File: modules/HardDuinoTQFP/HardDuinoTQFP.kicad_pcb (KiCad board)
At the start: 2 copper layers, 40.6 x 40.6 mm, 6 parts, among them J1 Conn_01x10_Male, J2 Conn_01x10_Male

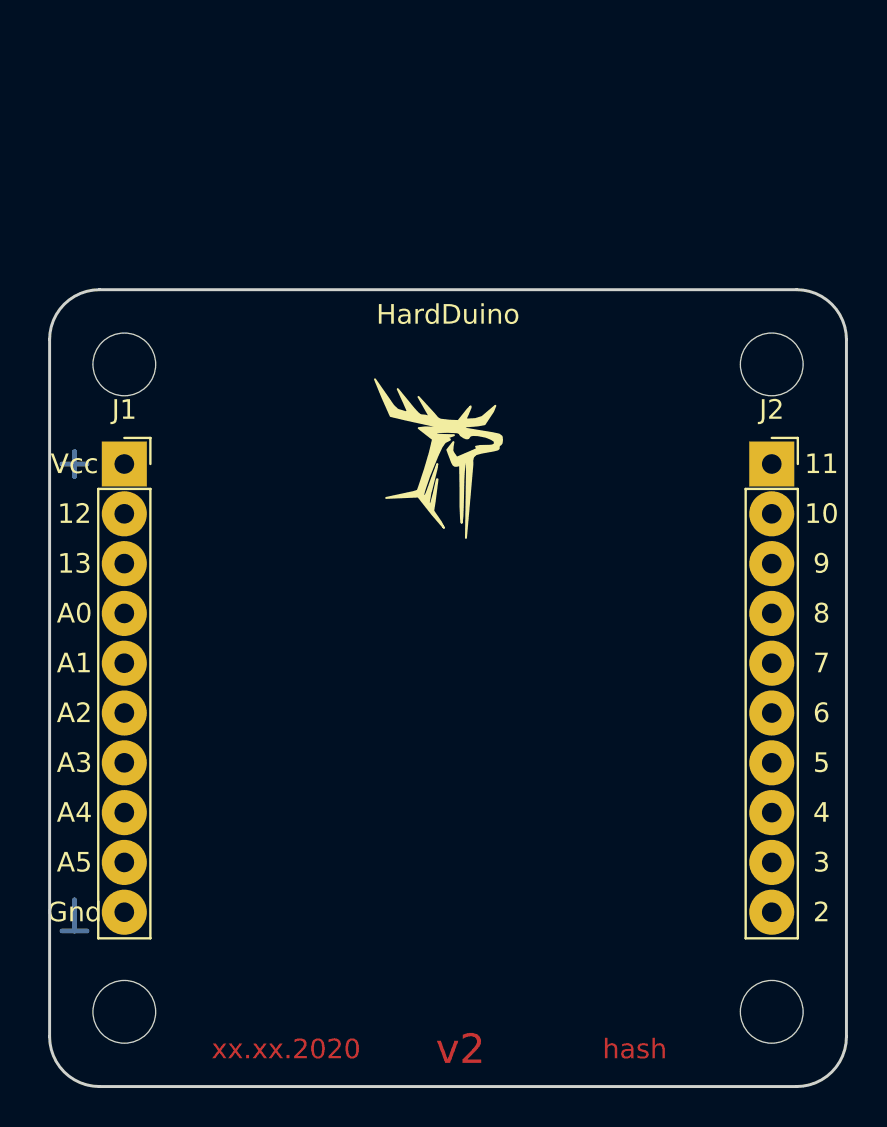
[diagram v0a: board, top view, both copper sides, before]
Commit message: HardDuino TQFP is ready
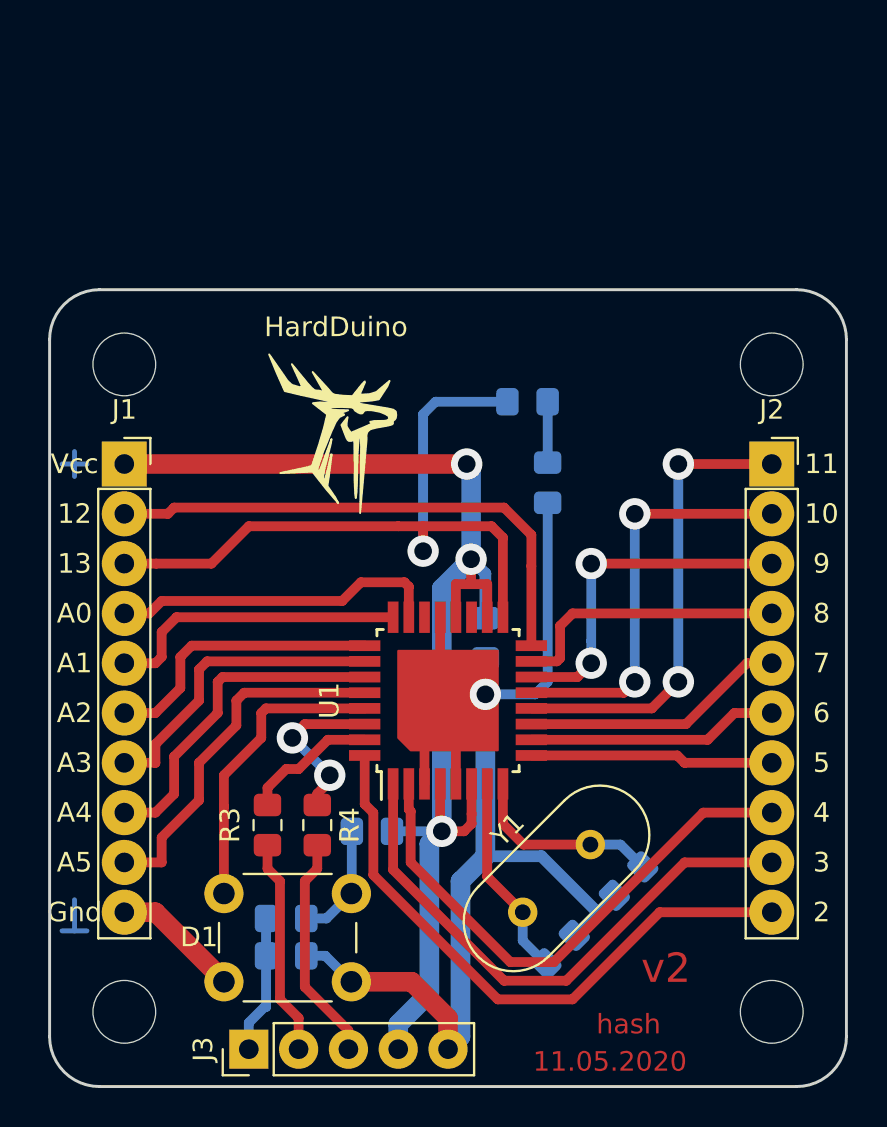
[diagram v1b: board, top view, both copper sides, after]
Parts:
- added C1: 0.1uF, Capacitor_SMD:C_0805_2012Metric_Pad1.15x1.40mm_HandSolder, B.Cu at (101.0, 82.9)
- added C2: 22pF, Capacitor_SMD:C_0805_2012Metric_Pad1.15x1.40mm_HandSolder, B.Cu at (114.9, 84.5)
- added C3: 22pF, Capacitor_SMD:C_0805_2012Metric_Pad1.15x1.40mm_HandSolder, B.Cu at (118.4, 81.0)
- added C4: C, Capacitor_SMD:C_0805_2012Metric_Pad1.15x1.40mm_HandSolder, B.Cu at (111.1, 68.6)
- added D1: 6x6-tact-btn, CommonLibrary:6x6-tact-btn, F.Cu at (97.8, 81.6)
- added D2: LED, LED_SMD:LED_0805_2012Metric_Pad1.15x1.40mm_HandSolder, B.Cu at (113.3, 56.5)
- added J3: Conn_01x05_Male, Connector_PinHeader_2.54mm:PinHeader_1x05_P2.54mm_Vertical, F.Cu at (99.1, 89.5)
- added R1: 1k, Resistor_SMD:R_0805_2012Metric_Pad1.15x1.40mm_HandSolder, B.Cu at (114.3, 60.6)
- added R2: 1k, Resistor_SMD:R_0805_2012Metric_Pad1.15x1.40mm_HandSolder, B.Cu at (101.0, 84.8)
- added R3: 1k, Resistor_SMD:R_0805_2012Metric_Pad1.15x1.40mm_HandSolder, F.Cu at (100.0, 78.1)
- added R4: 1k, Resistor_SMD:R_0805_2012Metric_Pad1.15x1.40mm_HandSolder, F.Cu at (102.6, 78.1)
- added R5: 10k, Resistor_SMD:R_0805_2012Metric_Pad1.15x1.40mm_HandSolder, B.Cu at (105.3, 78.4)
- added U1: ATmega328P-AU, Package_QFP:TQFP-32_7x7mm_P0.8mm, F.Cu at (109.2, 71.8)
- added Y1: 16MHz, Crystal:Crystal_HC49-U_Vertical, F.Cu at (113.0, 82.5)
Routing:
- net GND: track 0.00 -> 78.8 mm, vias 0 -> 1
- net VCC: track 0.00 -> 67.5 mm, vias 0 -> 3
- net /13: track 0.00 -> 37.2 mm, vias 0 -> 1
- net /2: track 0.00 -> 31.1 mm
- net /3: track 0.00 -> 28.5 mm
- net /4: track 0.00 -> 27.7 mm
- net /12: track 0.00 -> 27.1 mm
- net /11: track 0.00 -> 23.9 mm, vias 0 -> 2
- net Net-(C1-Pad1): track 0.00 -> 21.4 mm
- net /10: track 0.00 -> 21.1 mm, vias 0 -> 2
- net /A5: track 0.00 -> 18.4 mm
- net /9: track 0.00 -> 17.6 mm, vias 0 -> 2
- net /A4: track 0.00 -> 17.2 mm
- net /A0: track 0.00 -> 16.8 mm
- net /A3: track 0.00 -> 15.9 mm
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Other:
- board text added: "11.05.2020"
- board text removed: "xx.xx.2020"

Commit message: HardDuino TQFP polishing
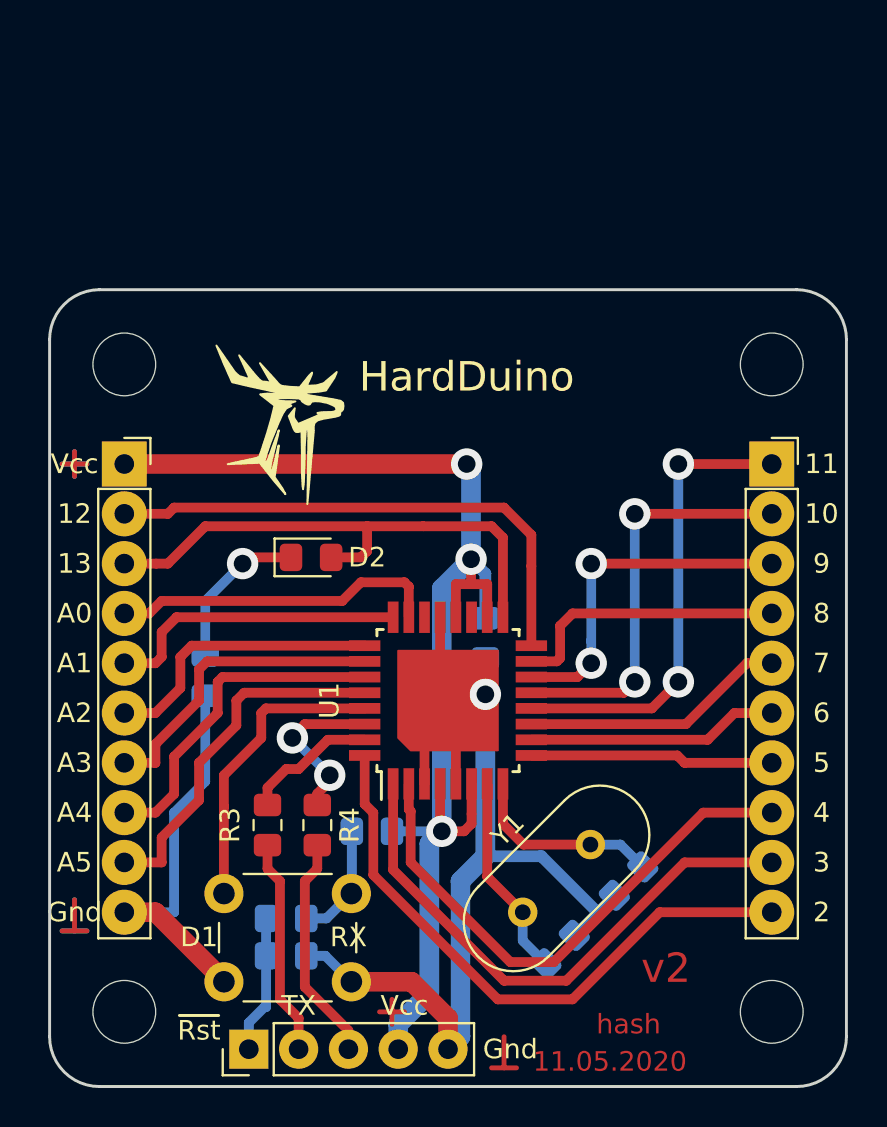
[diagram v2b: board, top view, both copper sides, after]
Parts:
- D2: moved to F.Cu
- moved R1 20.0 mm to (96.8, 70.5)
- moved D2 13.6 mm to (102.2, 64.5), turned to 0 degrees
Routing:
- net (no net): track 5.40 -> 16.2 mm
- net /13: track 37.2 -> 27.6 mm, vias 1 -> 0
- net Net-(D2-Pad1): track 3.10 -> 8.08 mm, vias 0 -> 1
- net GND: track 78.8 -> 80.7 mm
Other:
- board text added: "RX"
- board text added: "TX"
- board text added: "~Rst"

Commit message: Update hash
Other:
- board text added: "16.05.2020"
- board text added: "64baef"
- board text removed: "11.05.2020"
- board text removed: "hash"
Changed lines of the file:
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@@
   )
   (setup
-    (last_trace_width 0.5)
+    (last_trace_width 0.25)
     (user_trace_width 0.4)
     (user_trace_width 0.5)
@@
   )
   (gr_poly (pts (xy 111.76 74.295) (xy 107.315 74.295) (xy 106.68 73.66) (xy 106.68 69.215) (xy 111.76 69.215)) (layer F.Cu) (width 0.1))
-  (gr_text hash (at 118.4275 88.265) (layer F.Cu)
+  (gr_text 64baef (at 118.4275 88.265) (layer F.Cu)
     (effects (font (size 1 1) (thickness 0.2)))
   )
@@
     (effects (font (size 1.5 1.5) (thickness 0.3)))
   )
-  (gr_text 11.05.2020 (at 117.475 90.17) (layer F.Cu)
+  (gr_text 16.05.2020 (at 117.475 90.17) (layer F.Cu)
     (effects (font (size 1 1) (thickness 0.2)))
   )
@@
   (segment (start 106.9975 87.63) (end 105.7275 87.63) (width 0.25) (layer F.Cu) (net 0))
   (segment (start 106.3625 86.995) (end 106.3625 88.265) (width 0.25) (layer F.Cu) (net 0))
-  (via (at 98.7425 64.77) (size 1.6) (drill 0.9) (layers F.Cu B.Cu) (net 25))
   (via (at 108.9025 78.4225) (size 1.6) (drill 0.9) (layers F.Cu B.Cu) (net 1))
   (segment (start 109.62 67.505) (end 109.62 65.8175) (width 0.5) (layer F.Cu) (net 1))
@@
   (segment (start 118.013887 79.099319) (end 116.480681 79.099319) (width 0.5) (layer B.Cu) (net 24))
   (segment (start 119.152284 80.237716) (end 118.013887 79.099319) (width 0.5) (layer B.Cu) (net 24))
+  (via (at 98.7425 64.77) (size 1.6) (drill 0.9) (layers F.Cu B.Cu) (net 25))
   (segment (start 99.06 64.4525) (end 98.7425 64.77) (width 0.5) (layer F.Cu) (net 25))
   (segment (start 101.21 64.4525) (end 99.06 64.4525) (width 0.5) (layer F.Cu) (net 25))

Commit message: HardDuinoTQFP polishing
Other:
- board text added: "66a213"
- board text removed: "64baef"
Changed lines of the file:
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@@
     (nets 32)
   )
-  (page A4)
+  (page A4 portrait)
   (layers
     (0 F.Cu signal)
@@
     (visible_elements 7FFFFFFF)
     (pcbplotparams
-      (layerselection 0x010fc_ffffffff)
+      (layerselection 0x00000_fffffffe)
       (usegerberextensions false)
       (usegerberattributes false)
@@
       (hpglpenspeed 20)
       (hpglpendiameter 15.000000)
-      (psnegative false)
+      (psnegative true)
       (psa4output false)
       (plotreference true)
@@
       (padsonsilk false)
       (subtractmaskfromsilk false)
-      (outputformat 1)
+      (outputformat 4)
       (mirror false)
       (drillshape 1)
       (scaleselection 1)
-      (outputdirectory ""))
+      (outputdirectory "pdf/"))
   )
   (net 0 "")
@@
   )
   (gr_poly (pts (xy 111.76 74.295) (xy 107.315 74.295) (xy 106.68 73.66) (xy 106.68 69.215) (xy 111.76 69.215)) (layer F.Cu) (width 0.1))
-  (gr_text 64baef (at 118.4275 88.265) (layer F.Cu)
+  (gr_text 66a213 (at 118.4275 88.265) (layer F.Cu)
     (effects (font (size 1 1) (thickness 0.2)))
   )

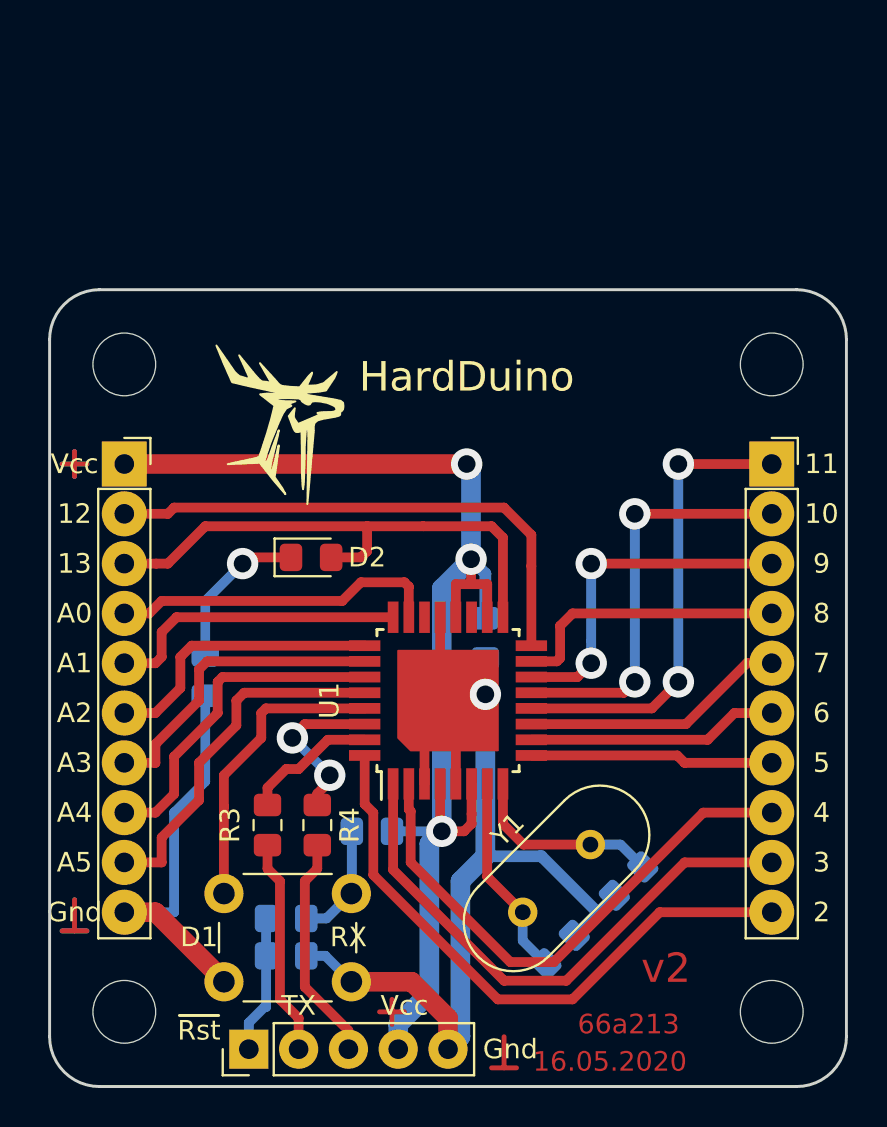
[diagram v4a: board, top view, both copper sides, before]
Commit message: HardDuinoTQFP. Move pcb, add photomask
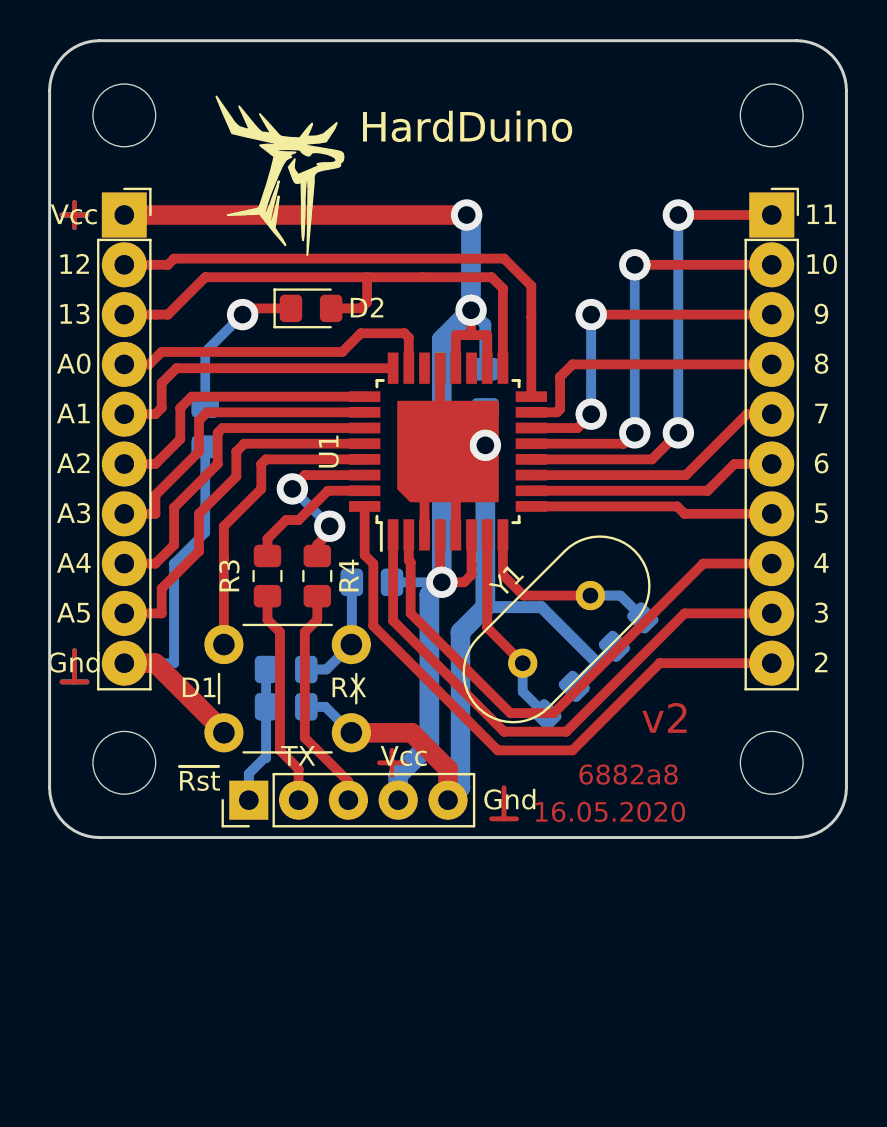
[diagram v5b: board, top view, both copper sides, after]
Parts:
- moved C1 12.7 mm to (101.0, 70.2)
- moved C2 12.7 mm to (114.9, 71.8)
- moved C3 12.7 mm to (118.4, 68.3)
- moved D1 12.7 mm to (97.8, 68.9)
- moved D2 12.7 mm to (102.2, 51.8)
- moved H1 12.7 mm to (92.7, 41.9)
- moved H3 12.7 mm to (125.7, 41.9)
- moved J3 12.7 mm to (99.1, 76.8)
- moved R1 12.7 mm to (96.8, 57.8)
- moved R3 12.7 mm to (100.0, 65.4)
- moved R4 12.7 mm to (102.6, 65.4)
- moved R5 12.7 mm to (105.3, 65.7)
- moved Y1 12.7 mm to (113.0, 69.8)
- moved C4 12.7 mm to (111.1, 55.9)
- moved J1 12.7 mm to (92.7, 47.0)
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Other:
- board text added: "6882a8"
- board text removed: "66a213"

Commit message: HardDuinoTQFP: fix pin numbering (8 and 12 was mixed up) Add ISP pinheader
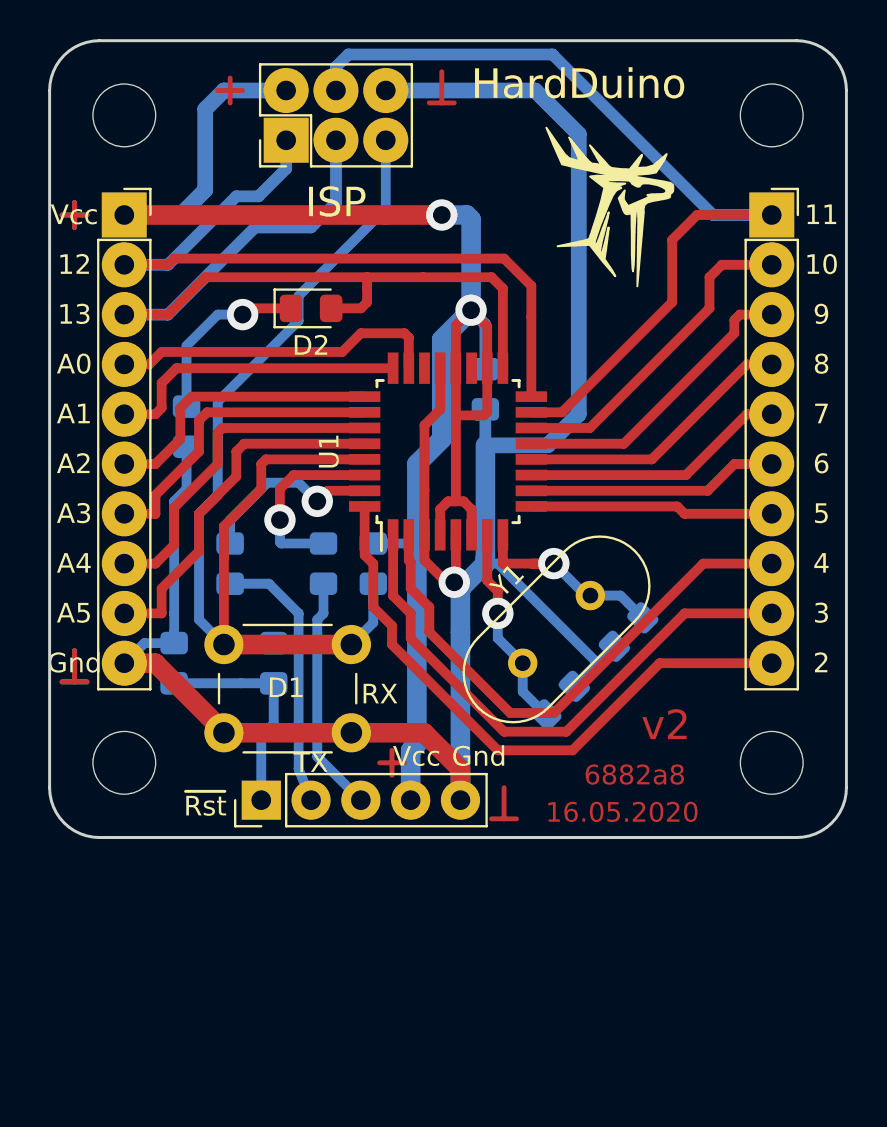
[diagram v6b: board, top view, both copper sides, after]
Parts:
- added J4: Conn_02x03_Odd_Even, Connector_PinHeader_2.54mm:PinHeader_2x03_P2.54mm_Vertical, F.Cu at (101.0, 43.2)
- R3, R4: moved to B.Cu
- moved R2 6.13 mm to (95.2, 69.8), turned to 270 degrees
- moved R3 2.01 mm to (98.1, 64.8)
- moved R5 0.96 mm to (105.4, 64.8), turned to 270 degrees
- moved R1 0.95 mm to (95.9, 57.8)
- moved C1 0.71 mm to (100.3, 69.8), turned to 270 degrees
- moved R4 0.71 mm to (102.9, 64.8)
- moved J3 0.63 mm to (99.7, 76.8)
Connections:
- net Net-(C1-Pad1) renamed /RST
- U1 pad 12: /11 -> /8
- U1 pad 13: /10 -> /9
- U1 pad 14: /9 -> /10
- U1 pad 15: /8 -> /11
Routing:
- net /RST: track 21.4 -> 58.2 mm
- net GND: track 80.7 -> 110.8 mm
- net VCC: track 67.5 -> 89.8 mm, vias 3 -> 2
- net /11: track 23.9 -> 45.4 mm, vias 2 -> 0
- net /13: track 27.6 -> 44.0 mm
- net /12: track 27.1 -> 38.9 mm
- net (no net): track 16.2 -> 21.6 mm
- net /10: track 21.1 -> 16.6 mm, vias 2 -> 0
- net /~RESET: track 7.08 -> 11.4 mm
- net /TX: track 11.1 -> 13.8 mm
- net Net-(R3-Pad1): track 6.85 -> 9.47 mm, vias 0 -> 1
- net /9: track 17.6 -> 15.4 mm, vias 2 -> 0
- net Net-(D2-Pad1): track 8.08 -> 9.22 mm
- net Net-(R4-Pad1): track 8.52 -> 9.58 mm, vias 2 -> 1
- net Net-(C3-Pad2): track 10.1 -> 10.9 mm, vias 0 -> 1
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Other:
- board text added: "ISP"
